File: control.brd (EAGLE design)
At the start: 186 x 186 mm, 103 parts, among them CN1 40PIN FPC, CN2 MINI B USB, CN3 2X10 HEADER, CN4 2X10 HEADER, SW1 TACT, SW10 TACT, SW11 TACT, SW12 TACT, SW13 TACT, SW14 TACT, SW15 TACT, SW16 TACT, SW2 TACT, SW3 TACT, SW4 TACT, SW5 TACT, SW6 TACT, SW7 TACT, SW8 TACT, SW9 TACT, U1 STM32H743ZI, U2 AS4C8M16SA, U3 TPS61169DCKR, U4 USBLC6-2SC6, U5 FT230X, U6 DCDC 3V3

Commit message: Updated libs with digikey numbers
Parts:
- U3: value TPS61169DCKR -> TPS61169
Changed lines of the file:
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@@
 <setting verticaltext="up"/>
 </settings>
-<grid distance="0.125" unitdist="mm" unit="mm" style="lines" multiple="1" display="yes" altdistance="0.125" altunitdist="mm" altunit="mm"/>
+<grid distance="0.25" unitdist="mm" unit="mm" style="lines" multiple="1" display="yes" altdistance="0.125" altunitdist="mm" altunit="mm"/>
 <layers>
 <layer number="1" name="Top" color="4" fill="1" visible="yes" active="yes"/>
@@
 </layers>
 <board>
-<fusionsync huburn="a.cGVyc29uYWw6dWUyYjllNWFm" projecturn="a.cGVyc29uYWw6dWUyYjllNWFmIzIwMjAwODI1MzI2NDUzNDMx" f3durn="urn:adsk.wipprod:dm.lineage:wnPGf6KyQv68ik76HDulcw" pcbguid="" lastpulledtime="" lastsyncedchangeguid="" latestrevisionid="06f15686-0416-4ee5-bf46-efffa6f91c55" lastsyncedrevisionid="06f15686-0416-4ee5-bf46-efffa6f91c55" lastboardhashguid="fab530b9-1610-bf14-5bc2-751c0d396012" lastpushedtime="2020-10-08T19:35:29Z" linktopcb3d="true"/>
+<fusionsync huburn="a.cGVyc29uYWw6dWUyYjllNWFm" projecturn="a.cGVyc29uYWw6dWUyYjllNWFmIzIwMjAwODI1MzI2NDUzNDMx" f3durn="urn:adsk.wipprod:dm.lineage:wnPGf6KyQv68ik76HDulcw" pcbguid="" lastpulledtime="" lastsyncedchangeguid="" latestrevisionid="7a307484-2ec1-4d7e-9476-243fbb9a2d07" lastsyncedrevisionid="7a307484-2ec1-4d7e-9476-243fbb9a2d07" lastboardhashguid="120816e1-c1dd-6910-7933-381bd53632a1" lastpushedtime="2020-10-09T08:12:07Z" linktopcb3d="true"/>
 <plain>
 <wire x1="90" y1="-93" x2="93" y2="-90" width="0" layer="20" curve="90" locked="yes"/>
@@
 <attribute name="PRICE_PER" value="0.14" x="-33.5" y="40.125" size="1.778" layer="28" rot="MR270" display="off"/>
 </element>
-<element name="U3" library="ICs" package="SOT23-5" value="TPS61169DCKR" x="-51" y="37.125" smashed="yes" rot="MR90">
-<attribute name="DIGIKEY" value="" x="-51" y="37.125" size="1.778" layer="28" rot="MR90" display="off"/>
-<attribute name="FARNELL" value="" x="-51" y="37.125" size="1.778" layer="28" rot="MR90" display="off"/>
+<element name="U3" library="ICs" package="SOT23-5" value="TPS61169" x="-51" y="37.125" smashed="yes" rot="MR90">
+<attribute name="DIGIKEY" value="296-40821-1-ND" x="-51" y="37.125" size="1.778" layer="28" rot="MR90" display="off"/>
+<attribute name="HEIGHT" value="2" x="-51" y="37.125" size="1.778" layer="28" rot="MR90" display="off"/>
 <attribute name="NAME" x="-48.75" y="35.625" size="1" layer="26" rot="MR90"/>
+<attribute name="PRICE_PER" value="0.7" x="-51" y="37.125" size="1.778" layer="28" rot="MR90" display="off"/>
+<attribute name="VALUE" value="TPS61169" x="-51" y="37.125" size="1.778" layer="28" rot="MR90" display="off"/>
 </element>
 <element name="U6" library="ICs" package="PDQE10" value="DCDC 3V3" x="80" y="35" smashed="yes" rot="MR180">
@@
 </element>
 <element name="C45" library="CAPACITORS" package="0603" value="4.7uF 6.3V" x="-53.75" y="40" smashed="yes" rot="MR270">
-<attribute name="FARNELL" value="2362095" x="-53.75" y="40" size="1.778" layer="28" rot="MR270" display="off"/>
+<attribute name="DIGIKEY" value="CL10B475KQ8NQNC" x="-53.75" y="40" size="1.778" layer="28" rot="MR270" display="off"/>
 <attribute name="HEIGHT" value="1" x="-53.75" y="40" size="1.778" layer="28" rot="MR270" display="off"/>
 <attribute name="NAME" x="-54.5" y="41.5" size="1.016" layer="26" rot="MR270"/>
-<attribute name="PRICE_PER" value="0.0414" x="-53.75" y="40" size="1.778" layer="28" rot="MR270" display="off"/>
+<attribute name="PRICE_PER" value="013" x="-53.75" y="40" size="1.778" layer="28" rot="MR270" display="off"/>
 </element>
 <element name="L1" library="INDUCTORS" package="SRN6045" value="4.7uH" x="-49.625" y="41.875" smashed="yes" rot="MR180">
@@
 </element>
 <element name="D1" library="DIODES" package="SOD128" value="3A 0.77V" x="-41.375" y="35.75" smashed="yes" rot="MR270">
-<attribute name="FARNELL" value="2498548" x="-41.375" y="35.75" size="1.778" layer="28" rot="MR270" display="off"/>
+<attribute name="DIGIKEY" value="1727-2397-1-ND" x="-41.375" y="35.75" size="1.778" layer="28" rot="MR270" display="off"/>
+<attribute name="HEIGHT" value="3" x="-41.375" y="35.75" size="1.778" layer="28" rot="MR270" display="off"/>
 <attribute name="NAME" x="-39.625" y="32.75" size="1" layer="26" rot="MR90"/>
-<attribute name="PRICE_PER" value="0.236" x="-41.375" y="35.75" size="1.778" layer="28" rot="MR270" display="off"/>
+<attribute name="PRICE_PER" value="0.37" x="-41.375" y="35.75" size="1.778" layer="28" rot="MR270" display="off"/>
 </element>
 <element name="C46" library="CAPACITORS" package="0603" value="1uF 25V" x="-41.375" y="31.125" smashed="yes" rot="MR90">

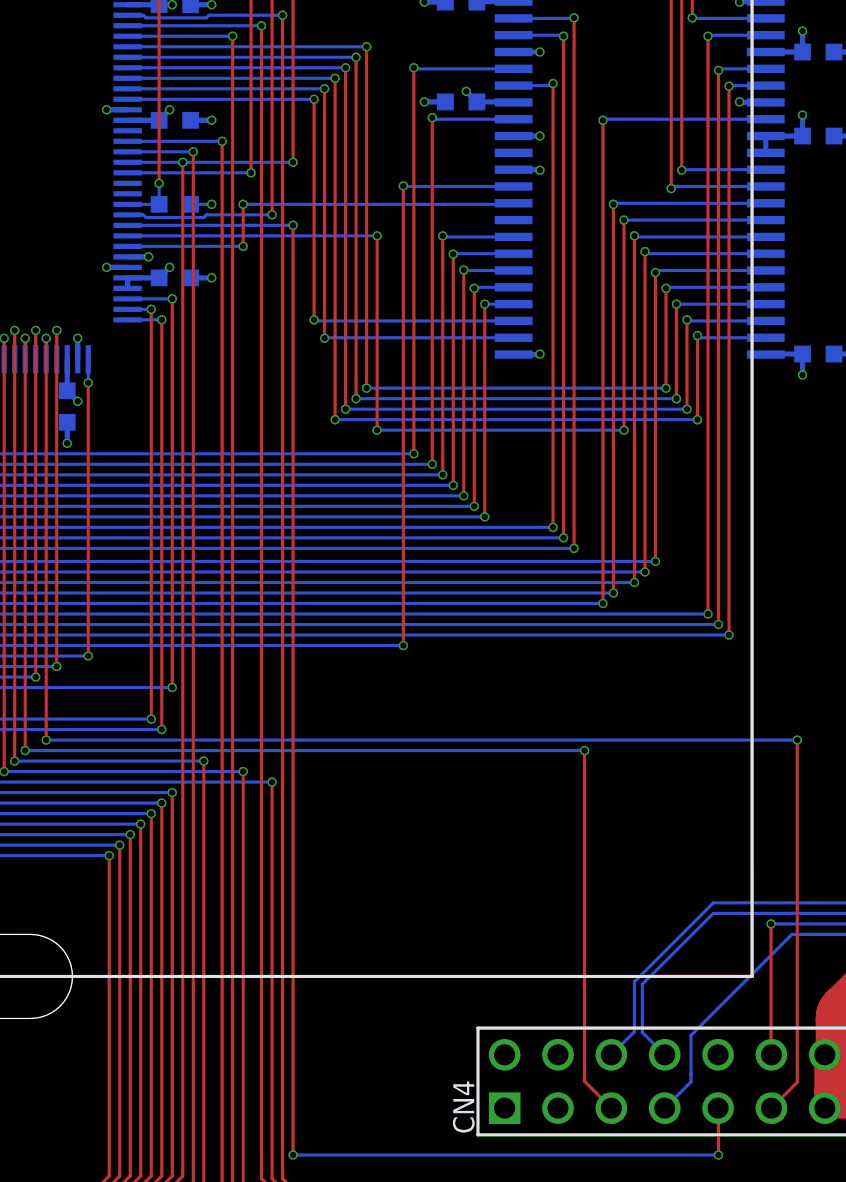
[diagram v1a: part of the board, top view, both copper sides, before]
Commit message: Added control for the output relay
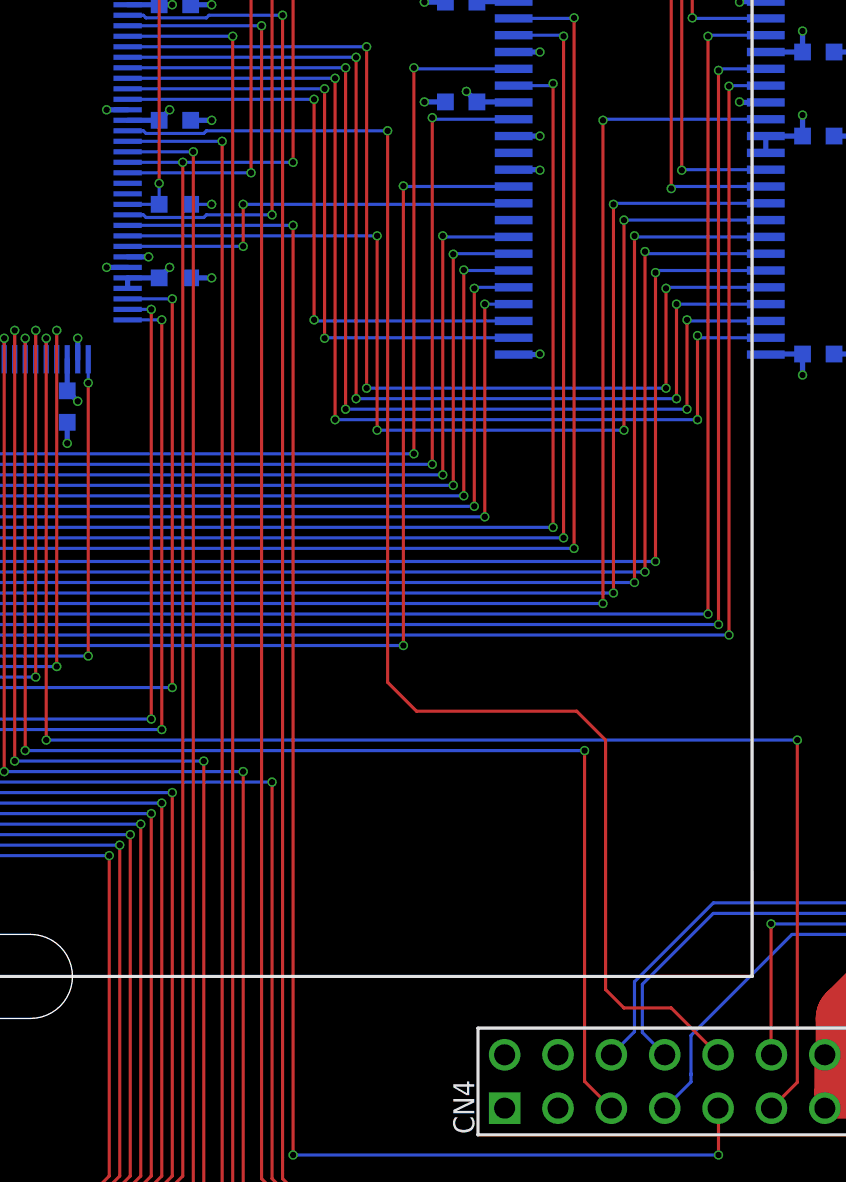
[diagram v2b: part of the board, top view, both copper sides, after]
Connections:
- new net OUTPUT_RELAY_EN: CN4.16, U1.18
- net GND: no longer CN4.16
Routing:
- net OUTPUT_RELAY_EN: track 0.00 -> 68.8 mm, vias 0 -> 1
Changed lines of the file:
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@@
 <setting verticaltext="up"/>
 </settings>
-<grid distance="0.25" unitdist="mm" unit="mm" style="lines" multiple="1" display="yes" altdistance="0.125" altunitdist="mm" altunit="mm"/>
+<grid distance="0.125" unitdist="mm" unit="mm" style="lines" multiple="1" display="yes" altdistance="0.125" altunitdist="mm" altunit="mm"/>
 <layers>
 <layer number="1" name="Top" color="4" fill="1" visible="yes" active="yes"/>
@@
 </layers>
 <board>
-<fusionsync huburn="a.cGVyc29uYWw6dWUyYjllNWFm" projecturn="a.cGVyc29uYWw6dWUyYjllNWFmIzIwMjAwODI1MzI2NDUzNDMx" f3durn="urn:adsk.wipprod:dm.lineage:wnPGf6KyQv68ik76HDulcw" pcbguid="" lastpulledtime="" lastsyncedchangeguid="" latestrevisionid="7a307484-2ec1-4d7e-9476-243fbb9a2d07" lastsyncedrevisionid="7a307484-2ec1-4d7e-9476-243fbb9a2d07" lastboardhashguid="120816e1-c1dd-6910-7933-381bd53632a1" lastpushedtime="2020-10-09T08:12:07Z" linktopcb3d="true"/>
+<fusionsync huburn="a.cGVyc29uYWw6dWUyYjllNWFm" projecturn="a.cGVyc29uYWw6dWUyYjllNWFmIzIwMjAwODI1MzI2NDUzNDMx" f3durn="urn:adsk.wipprod:dm.lineage:wnPGf6KyQv68ik76HDulcw" pcbguid="" lastpulledtime="" lastsyncedchangeguid="" latestrevisionid="2ca1d1ef-4991-43c0-8b65-6e747995f1e9" lastsyncedrevisionid="2ca1d1ef-4991-43c0-8b65-6e747995f1e9" lastboardhashguid="514c7081-e8dd-fae7-9cc8-94f32975e53f" lastpushedtime="2020-10-09T13:18:08Z" linktopcb3d="true"/>
 <plain>
 <wire x1="90" y1="-93" x2="93" y2="-90" width="0" layer="20" curve="90" locked="yes"/>
@@
 <contactref element="CN4" pad="1"/>
 <contactref element="CN4" pad="20"/>
-<contactref element="CN4" pad="16"/>
 <wire x1="-61.875" y1="84.625" x2="-60.875" y2="84.625" width="0.15" layer="16"/>
 <via x="-60.875" y="84.625" extent="1-16" drill="0.3"/>
@@
 <wire x1="65.58" y1="-0.5" x2="63.81" y2="-0.5" width="1" layer="1"/>
 </signal>
+<signal name="OUTPUT_RELAY_EN">
+<contactref element="CN4" pad="16"/>
+<contactref element="U1" pad="18"/>
+<wire x1="30.625" y1="45.25" x2="31.375" y2="45.25" width="0.15" layer="16"/>
+<wire x1="31.375" y1="45.25" x2="31.5" y2="45.125" width="0.15" layer="16"/>
+<wire x1="31.5" y1="45.125" x2="34.25" y2="45.125" width="0.15" layer="16"/>
+<wire x1="34.25" y1="45.125" x2="34.375" y2="45.25" width="0.15" layer="16"/>
+<wire x1="34.375" y1="45.25" x2="43" y2="45.25" width="0.15" layer="16"/>
+<via x="43" y="45.25" extent="1-16" drill="0.3"/>
+<wire x1="43" y1="45.25" x2="43" y2="19" width="0.15" layer="1"/>
+<wire x1="44.375" y1="17.625" x2="52" y2="17.625" width="0.15" layer="1"/>
+<wire x1="52" y1="17.625" x2="53.375" y2="16.25" width="0.15" layer="1"/>
+<wire x1="54.25" y1="3.5" x2="56.5" y2="3.5" width="0.15" layer="1"/>
+<wire x1="56.5" y1="3.5" x2="58.73" y2="1.27" width="0.15" layer="1"/>
+<wire x1="43" y1="19" x2="44.375" y2="17.625" width="0.15" layer="1"/>
+<wire x1="53.375" y1="16.25" x2="53.375" y2="4.375" width="0.15" layer="1"/>
+<wire x1="53.375" y1="4.375" x2="54.25" y2="3.5" width="0.15" layer="1"/>
+</signal>
 </signals>
